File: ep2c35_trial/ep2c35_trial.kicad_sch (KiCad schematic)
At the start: 139 parts, among them J1 Conn_02x21_Odd_Even, J2 Conn_02x21_Odd_Even, J3 3M_8540-4500PL, J4 USB3_B_Micro_Amphenol_GSB343K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, J5 Conn_02x05_Odd_Even, J6 Conn_01x02_Male, J7 Conn_01x02_Male, J8 Conn_01x02_Male, J9 Conn_01x02_Male, U1 EP2C5F484, U2 MIC37302, U3 FT600Q-B-T, U4 W25Q16JVSNIQ, U5 MIC39102, U6 MIC49150-1.2, X1 FNETHE025, Y1 ABM7-30.000MHZ-D2Y-T

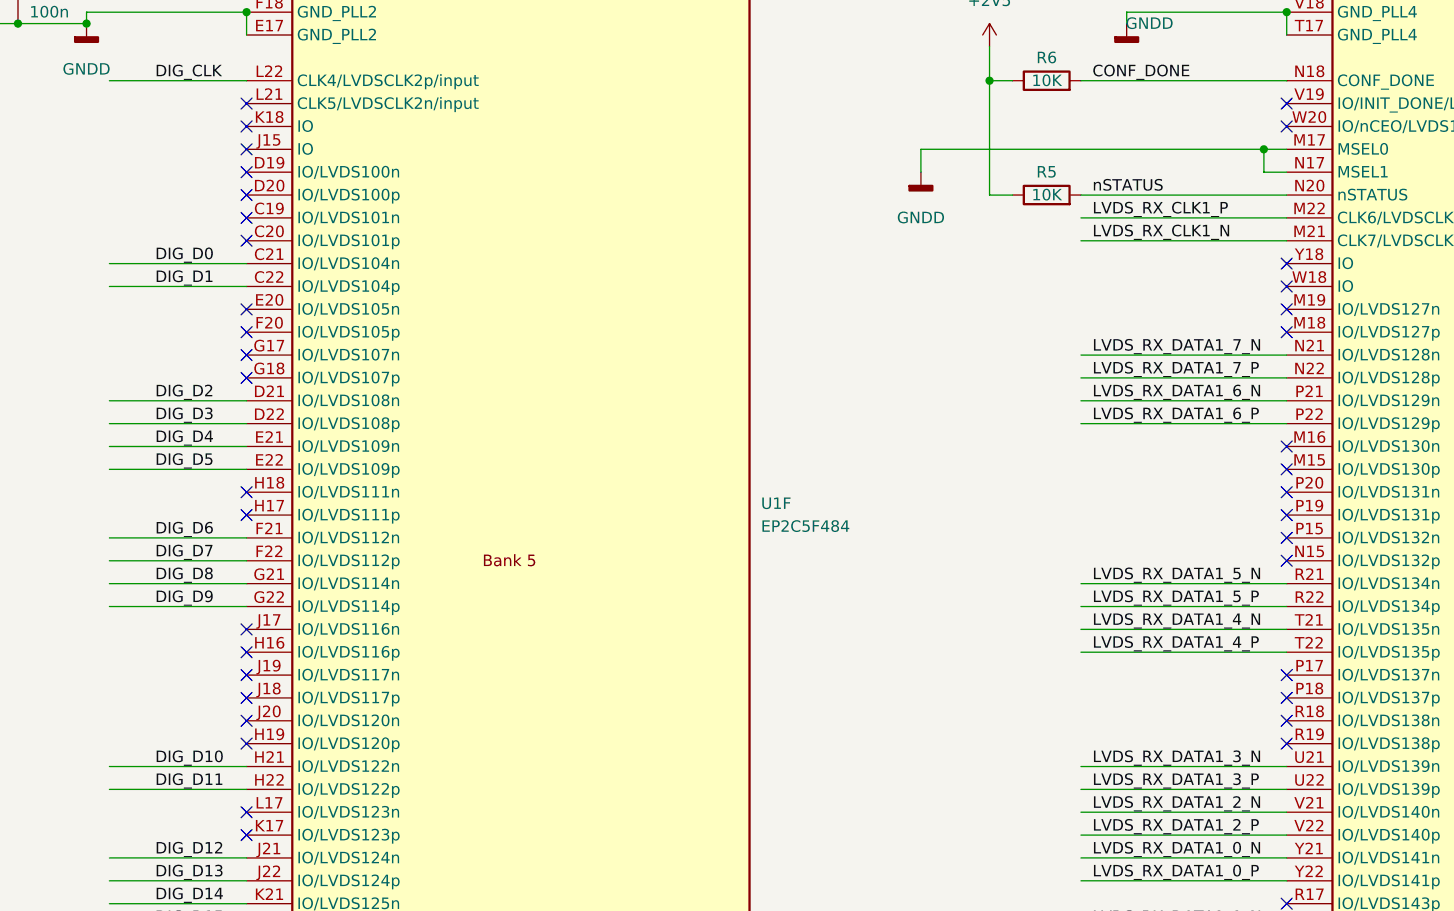
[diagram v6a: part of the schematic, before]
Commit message: Create assembly file. WIP.
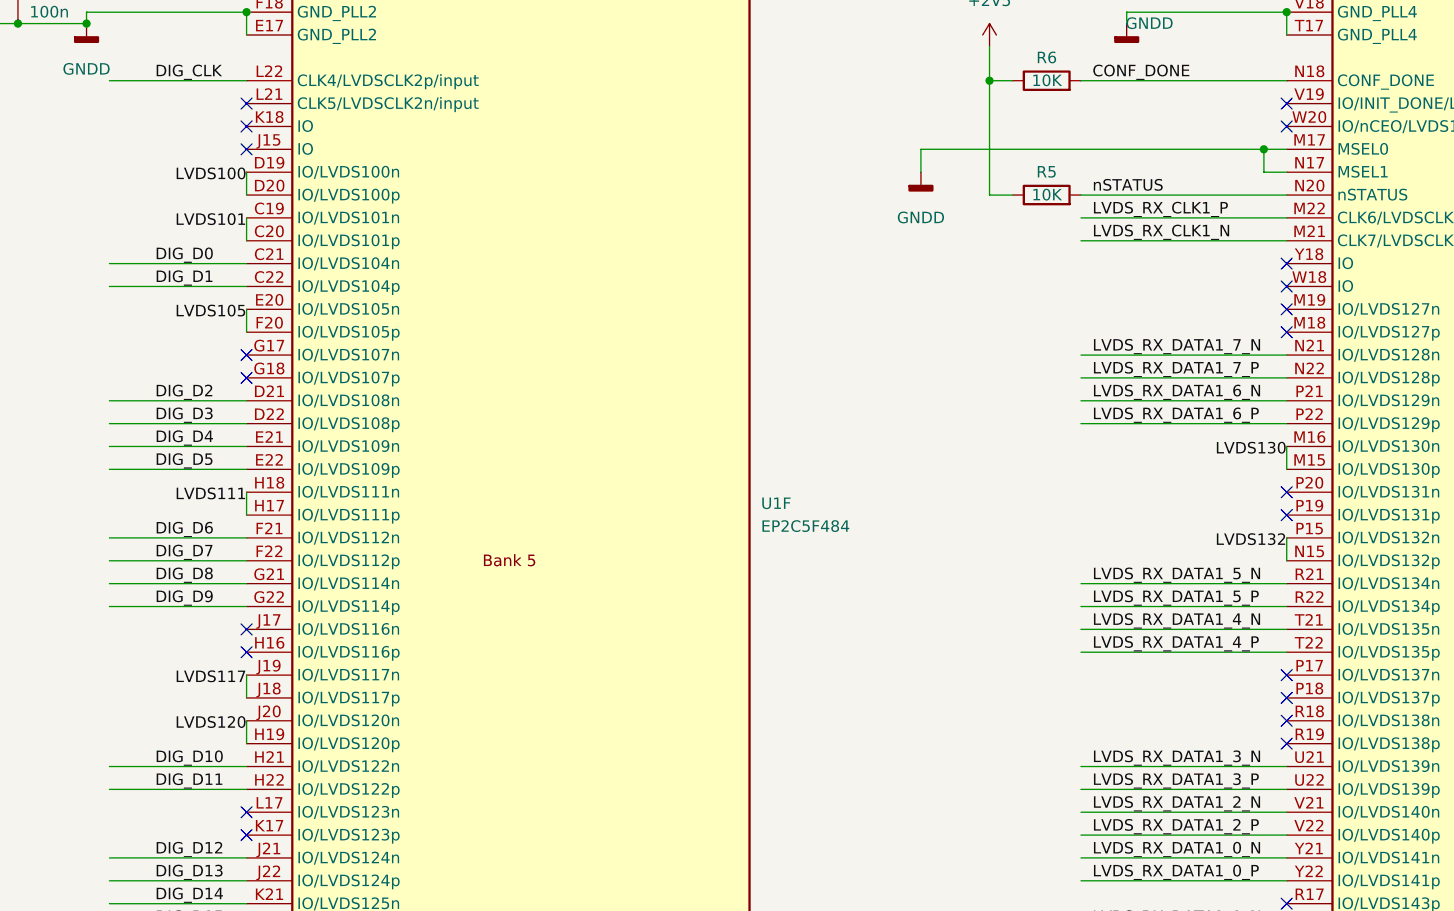
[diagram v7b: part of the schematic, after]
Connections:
- net LVDS101: now reaches U1.C19 (IO/LVDS101n)
- net LVDS101: now also U1.C20 (IO/LVDS101p)
- net LVDS100: now reaches U1.D19 (IO/LVDS100n)
- net LVDS100: now also U1.D20 (IO/LVDS100p)
- net LVDS105: now reaches U1.E20 (IO/LVDS105n)
- net LVDS105: now also U1.F20 (IO/LVDS105p)
- net LVDS111: now reaches U1.H17 (IO/LVDS111p)
- net LVDS111: now also U1.H18 (IO/LVDS111n)
- net LVDS120: now reaches U1.H19 (IO/LVDS120p)
- net LVDS120: now also U1.J20 (IO/LVDS120n)
- net LVDS117: now reaches U1.J18 (IO/LVDS117p)
- net LVDS117: now also U1.J19 (IO/LVDS117n)
- net LVDS130: now reaches U1.M15 (IO/LVDS130p)
- net LVDS130: now also U1.M16 (IO/LVDS130n)
- net LVDS132: now reaches U1.N15 (IO/LVDS132p)
- net LVDS132: now also U1.P15 (IO/LVDS132n)
- no-connect marks 212 -> 196
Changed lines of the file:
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@@
   (no_connect (at 265.43 87.63))
   (no_connect (at 265.43 260.35))
-  (no_connect (at 149.86 207.01))
   (no_connect (at 372.11 203.2))
   (no_connect (at 505.46 121.92))
@@
   (no_connect (at 505.46 58.42))
   (no_connect (at 372.11 223.52))
-  (no_connect (at 149.86 234.95))
   (no_connect (at 372.11 271.78))
   (no_connect (at 506.73 281.94))
@@
   (no_connect (at 265.43 82.55))
   (no_connect (at 372.11 215.9))
-  (no_connect (at 149.86 199.39))
   (no_connect (at 372.11 228.6))
   (no_connect (at 506.73 228.6))
@@
   (no_connect (at 265.43 156.21))
   (no_connect (at 375.92 110.49))
-  (no_connect (at 149.86 214.63))
   (no_connect (at 506.73 287.02))
   (no_connect (at 265.43 128.27))
   (no_connect (at 506.73 266.7))
-  (no_connect (at 149.86 257.81))
   (no_connect (at 506.73 276.86))
   (no_connect (at 505.46 101.6))
@@
   (no_connect (at 265.43 105.41))
   (no_connect (at 375.92 46.99))
-  (no_connect (at 149.86 237.49))
   (no_connect (at 265.43 306.07))
   (no_connect (at 372.11 233.68))
@@
   (no_connect (at 265.43 194.31))
   (no_connect (at 505.46 104.14))
-  (no_connect (at 149.86 201.93))
   (no_connect (at 372.11 259.08))
-  (no_connect (at 149.86 260.35))
   (no_connect (at 505.46 71.12))
-  (no_connect (at 149.86 217.17))
   (no_connect (at 505.46 66.04))
   (no_connect (at 372.11 226.06))
@@
   (no_connect (at 506.73 208.28))
   (no_connect (at 505.46 45.72))
-  (no_connect (at 265.43 240.03))
   (no_connect (at 265.43 102.87))
   (no_connect (at 265.43 125.73))
@@
   (no_connect (at 505.46 116.84))
   (no_connect (at 375.92 69.85))
-  (no_connect (at 149.86 204.47))
   (no_connect (at 265.43 130.81))
-  (no_connect (at 265.43 242.57))
   (no_connect (at 505.46 50.8))
   (no_connect (at 149.86 222.25))
@@
   (no_connect (at 476.25 323.85))
   (no_connect (at 506.73 203.2))
-  (no_connect (at 265.43 229.87))
   (no_connect (at 265.43 95.25))
   (no_connect (at 372.11 261.62))
@@
   (no_connect (at 505.46 114.3))
   (no_connect (at 265.43 97.79))
-  (no_connect (at 149.86 255.27))
   (no_connect (at 283.21 452.12))
   (no_connect (at 505.46 81.28))
   (no_connect (at 506.73 254))
   (no_connect (at 265.43 209.55))
-  (no_connect (at 265.43 232.41))
   (no_connect (at 372.11 256.54))
-  (no_connect (at 149.86 262.89))
   (no_connect (at 265.43 212.09))
   (no_connect (at 505.46 99.06))
@@
     (stroke (width 0) (type default) (color 0 0 0 0))
   )
+  (wire (pts (xy 265.43 240.03) (xy 265.43 242.57))
+    (stroke (width 0) (type default) (color 0 0 0 0))
+  )
   (wire (pts (xy 152.4 35.56) (xy 114.3 35.56))
     (stroke (width 0) (type default) (color 0 0 0 0))
@@
     (stroke (width 0) (type default) (color 0 0 0 0))
   )
+  (wire (pts (xy 149.86 199.39) (xy 149.86 201.93))
+    (stroke (width 0) (type default) (color 0 0 0 0))
+  )
   (wire (pts (xy 149.86 176.53) (xy 132.08 176.53))
     (stroke (width 0) (type default) (color 0 0 0 0))
@@
     (stroke (width 0) (type default) (color 0 0 0 0))
   )
+  (wire (pts (xy 149.86 214.63) (xy 149.86 217.17))
+    (stroke (width 0) (type default) (color 0 0 0 0))
+  )
   (wire (pts (xy 67.31 568.96) (xy 77.47 568.96))
     (stroke (width 0) (type default) (color 0 0 0 0))
@@
     (stroke (width 0) (type default) (color 0 0 0 0))
   )
+  (wire (pts (xy 149.86 260.35) (xy 149.86 262.89))
+    (stroke (width 0) (type default) (color 0 0 0 0))
+  )
   (wire (pts (xy 172.72 327.66) (xy 200.66 327.66))
     (stroke (width 0) (type default) (color 0 0 0 0))
@@
     (stroke (width 0) (type default) (color 0 0 0 0))
   )
+  (wire (pts (xy 149.86 234.95) (xy 149.86 237.49))
+    (stroke (width 0) (type default) (color 0 0 0 0))
+  )
   (wire (pts (xy 127 530.86) (xy 153.67 530.86))
     (stroke (width 0) (type default) (color 0 0 0 0))
@@
     (stroke (width 0) (type default) (color 0 0 0 0))
   )
+  (wire (pts (xy 149.86 255.27) (xy 149.86 257.81))
+    (stroke (width 0) (type default) (color 0 0 0 0))
+  )
   (wire (pts (xy 267.97 490.22) (xy 267.97 492.76))
     (stroke (width 0) (type default) (color 0 0 0 0))
@@
     (stroke (width 0) (type default) (color 0 0 0 0))
   )
+  (wire (pts (xy 265.43 229.87) (xy 265.43 232.41))
+    (stroke (width 0) (type default) (color 0 0 0 0))
+  )
   (wire (pts (xy 378.46 322.58) (xy 378.46 377.19))
     (stroke (width 0) (type default) (color 0 0 0 0))
@@
     (stroke (width 0) (type default) (color 0 0 0 0))
   )
+  (wire (pts (xy 149.86 204.47) (xy 149.86 207.01))
+    (stroke (width 0) (type default) (color 0 0 0 0))
+  )
   (wire (pts (xy 251.46 69.85) (xy 251.46 36.83))
     (stroke (width 0) (type default) (color 0 0 0 0))
@@
     (effects (font (size 1.27 1.27)) (justify left bottom))
   )
+  (label "LVDS111" (at 149.86 236.22 180)
+    (effects (font (size 1.27 1.27)) (justify right bottom))
+  )
   (label "LVDS_RX_DATA0_5_P" (at 275.59 342.9 0)
     (effects (font (size 1.27 1.27)) (justify left bottom))
@@
     (effects (font (size 1.27 1.27)) (justify left bottom))
   )
+  (label "LVDS101" (at 149.86 205.74 180)
+    (effects (font (size 1.27 1.27)) (justify right bottom))
+  )
   (label "LVDS_RX_DATA0_7_P" (at 128.27 314.96 0)
     (effects (font (size 1.27 1.27)) (justify left bottom))
@@
     (effects (font (size 1.27 1.27)) (justify left bottom))
   )
+  (label "LVDS105" (at 149.86 215.9 180)
+    (effects (font (size 1.27 1.27)) (justify right bottom))
+  )
   (label "LVDS_RX_FCLK1_P" (at 243.84 295.91 0)
     (effects (font (size 1.27 1.27)) (justify left bottom))
@@
     (effects (font (size 1.27 1.27)) (justify left bottom))
   )
+  (label "LVDS117" (at 149.86 256.54 180)
+    (effects (font (size 1.27 1.27)) (justify right bottom))
+  )
   (label "LVDS_RX_FCLK1_N" (at 358.14 365.76 0)
     (effects (font (size 1.27 1.27)) (justify left bottom))
@@
     (effects (font (size 1.27 1.27)) (justify left bottom))
   )
+  (label "LVDS130" (at 265.43 231.14 180)
+    (effects (font (size 1.27 1.27)) (justify right bottom))
+  )
   (label "USB_D_N" (at 449.58 539.75 0)
     (effects (font (size 1.27 1.27)) (justify left bottom))
@@
     (effects (font (size 1.27 1.27)) (justify left bottom))
   )
+  (label "LVDS100" (at 149.86 200.66 180)
+    (effects (font (size 1.27 1.27)) (justify right bottom))
+  )
   (label "DIG_D6" (at 139.7 240.03 0)
     (effects (font (size 1.27 1.27)) (justify left bottom))
@@
     (effects (font (size 1.27 1.27)) (justify left bottom))
   )
+  (label "LVDS120" (at 149.86 261.62 180)
+    (effects (font (size 1.27 1.27)) (justify right bottom))
+  )
   (label "LVDS_RX_DATA1_0_N" (at 243.84 275.59 0)
     (effects (font (size 1.27 1.27)) (justify left bottom))
@@
     (effects (font (size 1.27 1.27)) (justify left bottom))
   )
+  (label "LVDS132" (at 265.43 241.3 180)
+    (effects (font (size 1.27 1.27)) (justify right bottom))
+  )
   (label "FT_RXF_N" (at 360.68 105.41 0)

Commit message: Move JLCPCB components to bottom.
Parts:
- removed C21: 4.7u, Capacitor_SMD:C_0402_1005Metric, symbol Device:C
- added D1, D2, D3: LED, LED_SMD:LED_0603_1608Metric, symbol Device:LED
- added R49, R50, R51: 1k, Resistor_SMD:R_0402_1005Metric, symbol Device:R
- R2, R3, R4, R5, R6: value 10K -> 10k
- R8: value 10k -> 5k
- R9: value 10k -> 3k
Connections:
- net 1V2_LDO: now also D3.2 (A)
- net 2V5_LDO: now also D2.2 (A)
- net 3V3_LDO: now also D1.2 (A)
- net GND: now also R49.1, R50.1, R51.1
- net USB_D_N: now also U3.20 (DM); no longer U3.18 (DP)
- net USB_D_P: now also U3.18 (DP); no longer U3.20 (DM)
- new net: D2.1 (K), R50.2
- new net: D1.1 (K), R49.2
- new net: D3.1 (K), R51.2
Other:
- removed sheet EP2C35
- note added: "Vout=1.24(1+R1/R2) -> 2.48V"
- note added: "Vout=1.24(1+R1/R2) -> 3.3V"
- moved on the sheet: C13, C14, C29
